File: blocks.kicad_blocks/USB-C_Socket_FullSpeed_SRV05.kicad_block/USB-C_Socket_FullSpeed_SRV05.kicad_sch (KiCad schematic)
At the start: 4 parts, among them J2 TYPE-C-31-M-12, U1 SRV05-4

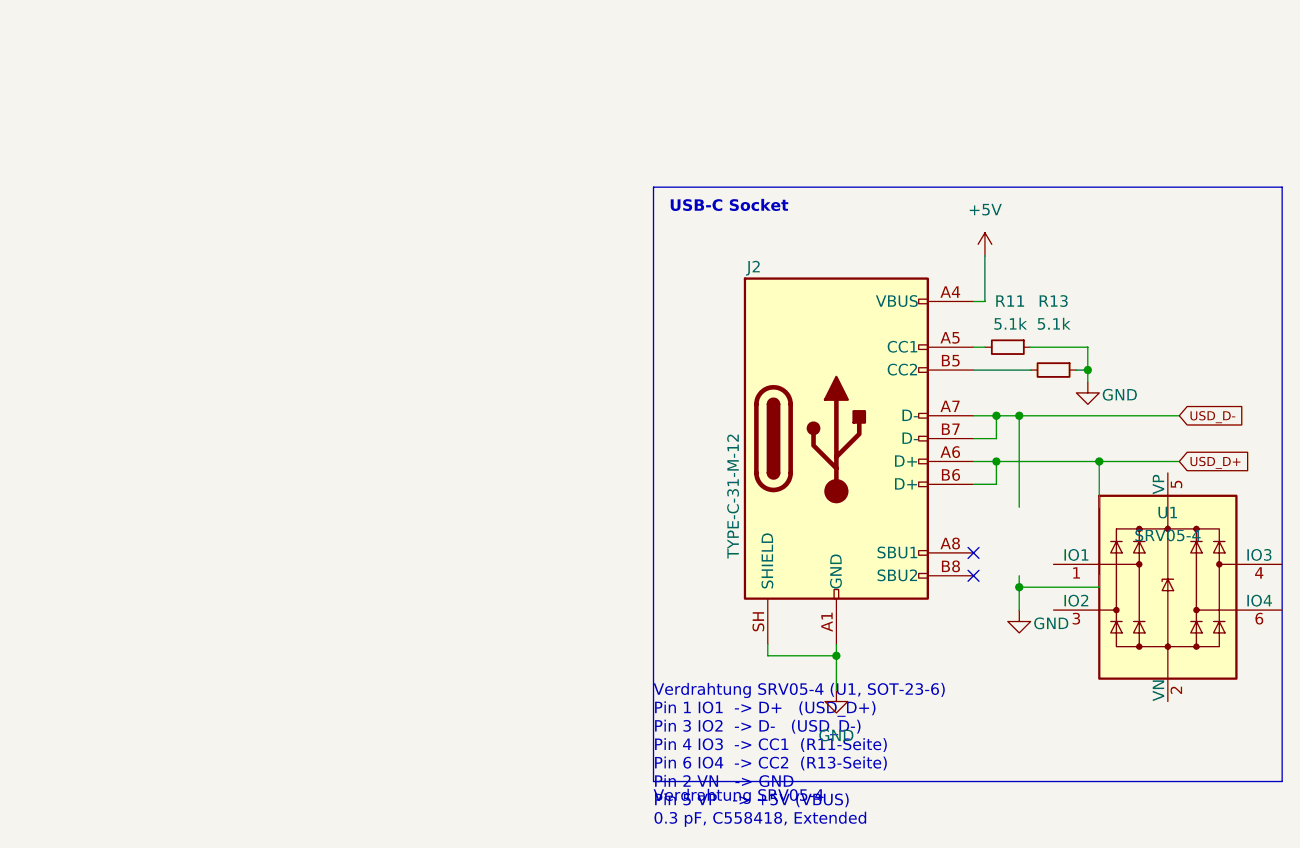
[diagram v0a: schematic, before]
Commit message: USB-C Socket FS (SRV05-4): Layout ergaenzt, Beschreibung und Metadaten vervollstaendigt (maturity layout, has_3d yes)
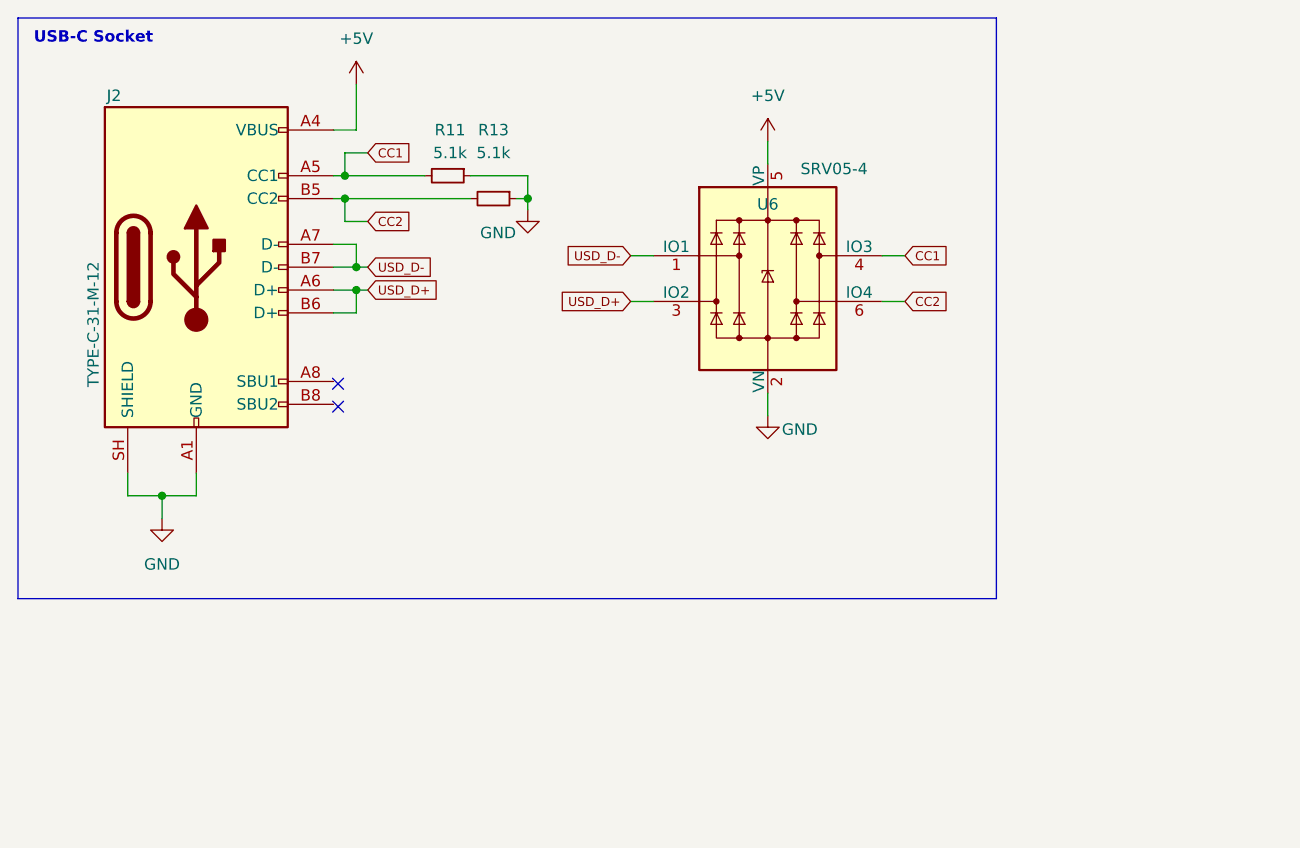
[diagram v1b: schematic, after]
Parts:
- renumbered U1 to U6
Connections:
- net +5V: now also U6.5 (VP)
- net GND: now also U6.2 (VN)
- net USD_D+: now also U6.3 (IO2)
- net USD_D-: now also U6.1 (IO1)
- net CC2: now reaches J2.B5 (CC2), R13.2
- net CC2: now also U6.6 (IO4)
- net CC1: now reaches J2.A5 (CC1), R11.2
- net CC1: now also U6.4 (IO3)
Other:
- note removed: "Verdrahtung SRV05-4"
- note removed: "Verdrahtung SRV05-4 (U1, SOT-23-6) Pin 1 IO1 -> D+ (USD_D+) Pin 3 IO2 -> D- (USD_D-) Pin 4 IO3 -> CC1 (R11-Seite) Pin 6 IO4 -> CC2 (R13-Seite) Pin 2 VN -> GND Pin 5 VP -> +5V (VBUS) 0.3 pF, C558418, Extended"
- moved on the sheet: J2, R11, R13, U6
